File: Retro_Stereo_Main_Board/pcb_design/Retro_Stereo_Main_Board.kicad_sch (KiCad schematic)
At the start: 2 parts, among them J1 Conn_02x15_Counter_Clockwise, U3 TPS65132WRVCR

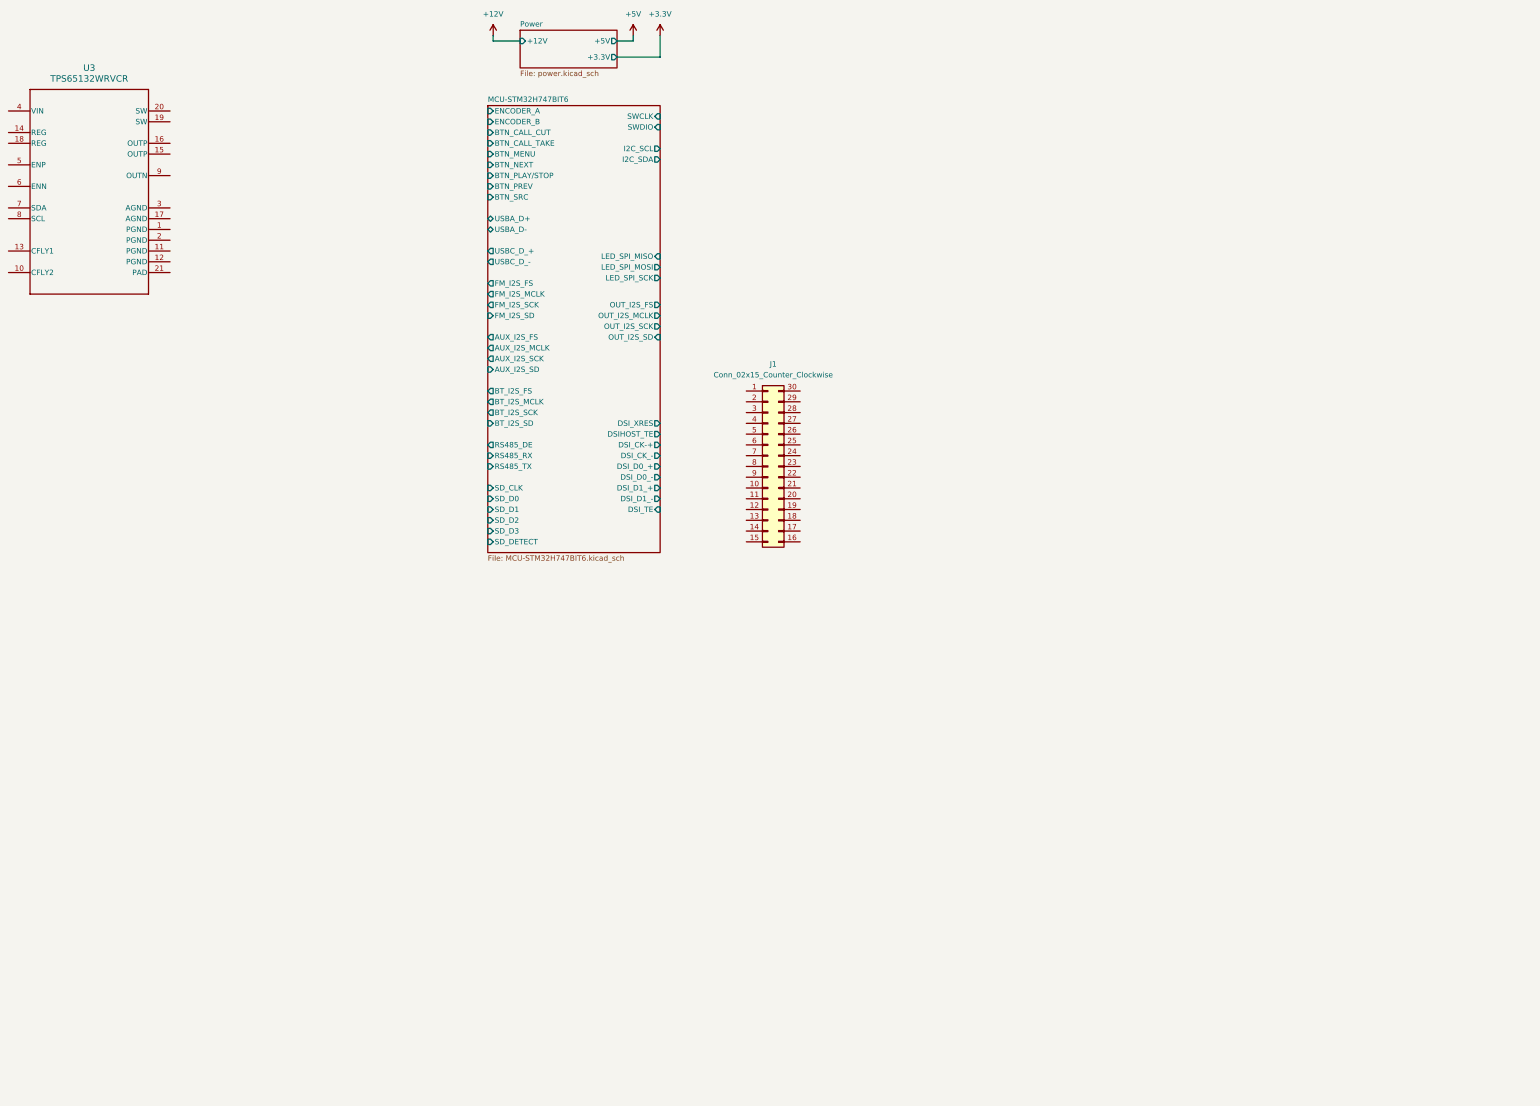
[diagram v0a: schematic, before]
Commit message: Define crystals, add peripherals
Signed-off-by: Francisco <fran.testa07Qgmail.com>
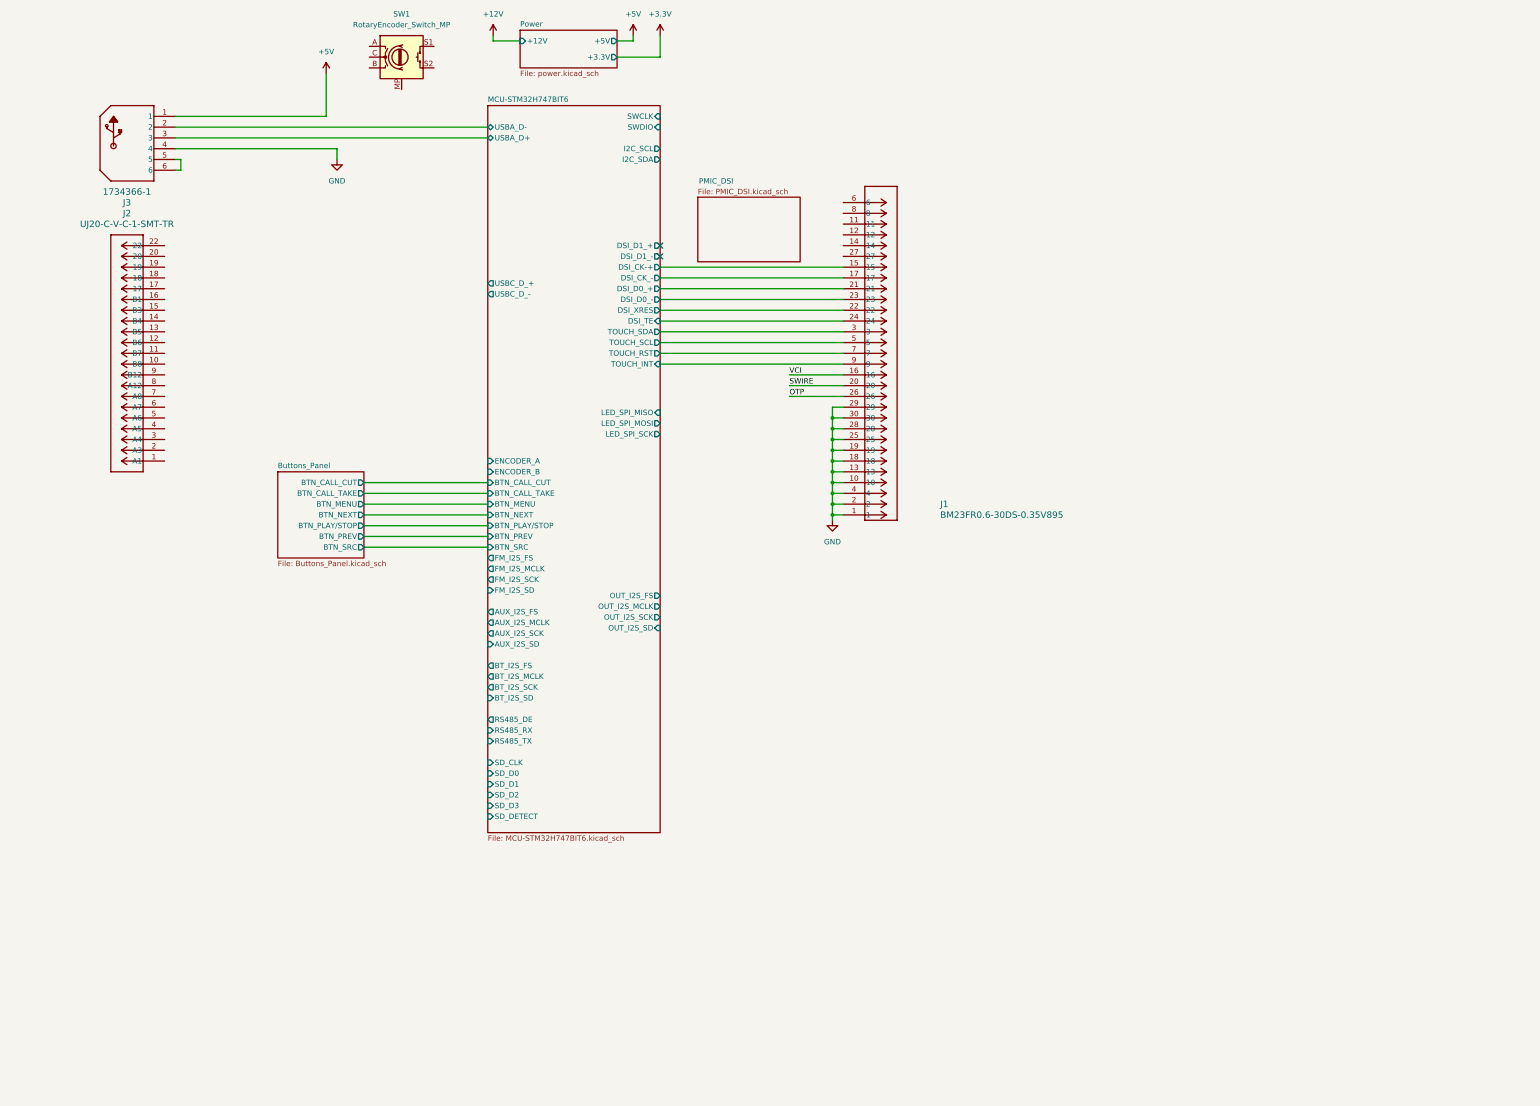
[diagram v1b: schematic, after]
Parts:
- removed J1: Conn_02x15_Counter_Clockwise, symbol Connector_Generic:Conn_02x15_Counter_Clockwise
- removed U3: TPS65132WRVCR, RVC0020A, symbol TPS65132WRVCR:TPS65132WRVCR
- added J1: BM23FR0.6-30DS-0.35V895, CONN_BM23FR0.6-30DS-0.35V895_HIR, symbol BM23FR0.6-30DS-0.35V(895):BM23FR0.6-30DS-0.35V895
- added J2: UJ20-C-V-C-1-SMT-TR, CONN8X2_UJ20-C-V-C-1-SMT-TR_CUD, symbol USBC_Samesky:UJ20-C-V-C-1-SMT-TR
- added J3: 1734366-1, CONN4_1734366-1_TEC, symbol USBA_TE:1734366-1
- added SW1: RotaryEncoder_Switch_MP, symbol Device:RotaryEncoder_Switch_MP
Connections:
- net +5V: now also J3.1
- net MCU-STM32H747BIT6/DSI_CK-+: now also J1.15
- net MCU-STM32H747BIT6/DSI_CK_-: now also J1.17
- net MCU-STM32H747BIT6/DSI_D0_+: now also J1.21
- net MCU-STM32H747BIT6/DSI_D0_-: now also J1.23
- net MCU-STM32H747BIT6/DSI_TE: now also J1.24
- net MCU-STM32H747BIT6/DSI_XRES: now also J1.22
- net MCU-STM32H747BIT6/USBA_D+: now also J3.3
- net MCU-STM32H747BIT6/USBA_D-: now also J3.2
- new net: J3.5, J3.6
- new net GND: J1.1, J1.10, J1.13, J1.18, J1.19, J1.2, J1.25, J1.28, J1.29, J1.30, J1.4, J3.4
- new net MCU-STM32H747BIT6/TOUCH_INT: J1.9
- new net MCU-STM32H747BIT6/TOUCH_RST: J1.7
- new net MCU-STM32H747BIT6/TOUCH_SCL: J1.5
- new net MCU-STM32H747BIT6/TOUCH_SDA: J1.3
- new net OTP: J1.26
- new net SWIRE: J1.20
- new net VCI: J1.16
- no-connect marks 0 -> 2
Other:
- added sheet Buttons_Panel (Buttons_Panel.kicad_sch)
- added sheet PMIC_DSI (PMIC_DSI.kicad_sch)
- sheet MCU-STM32H747BIT6 ports: added TOUCH_INT, TOUCH_RST, TOUCH_SCL, TOUCH_SDA; removed DSIHOST_TE

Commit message: Complete connections to display, add power block
Signed-off-by: Francisco <fran.testa07Qgmail.com>
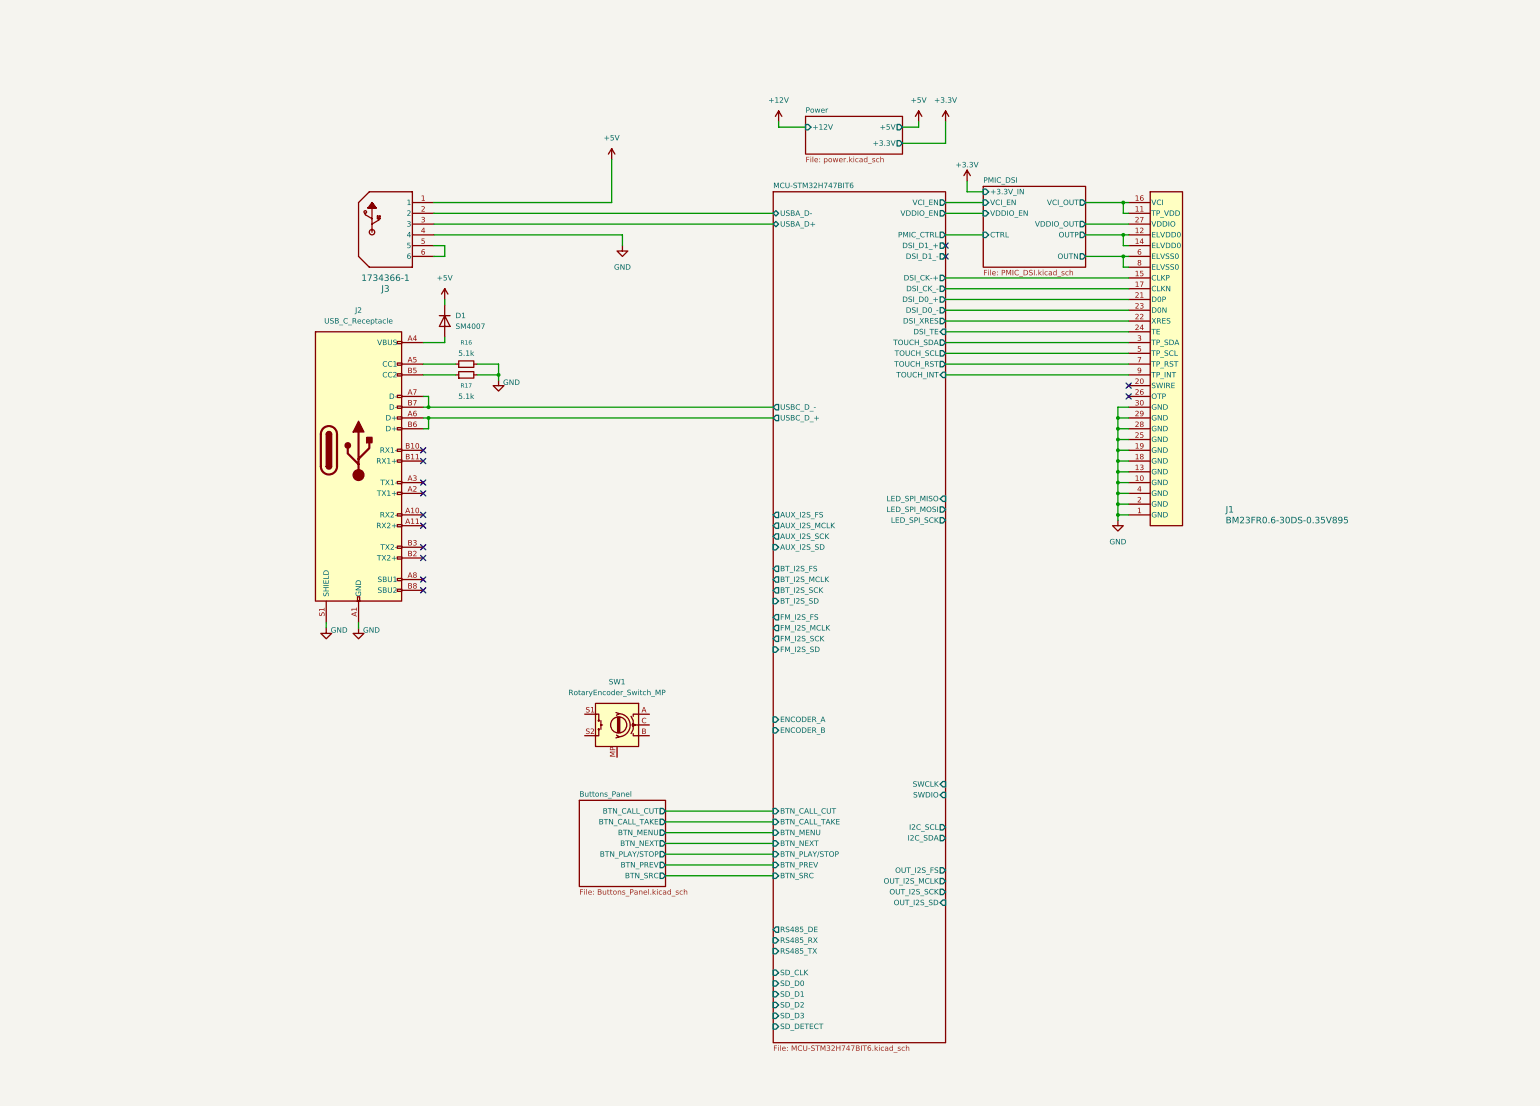
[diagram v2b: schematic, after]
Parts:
- removed J2: UJ20-C-V-C-1-SMT-TR, CONN8X2_UJ20-C-V-C-1-SMT-TR_CUD, symbol USBC_Samesky:UJ20-C-V-C-1-SMT-TR
- added D1: SM4007, Diode_SMD:D_SOD-123F, symbol Device:D
- added J2: USB_C_Receptacle, USBC_Samesky:CONN8X2_UJ20-C-V-C-1-SMT-TR_CUD, symbol Connector:USB_C_Receptacle
- added R16, R17: 5.1k, symbol Device:R_Small
- J3: footprint CONN4_1734366-1_TEC -> USBA_TE:CONN4_1734366-1_TEC
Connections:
- net VCI is gone; now on net PMIC_DSI/VCI_OUT: J1.16 (VCI)
- net +5V: now also D1.1 (K)
- net GND: now also J2.A1 (GND), J2.A12 (GND), J2.B1 (GND), J2.B12 (GND), J2.S1 (SHIELD), R16.2, R17.2
- net MCU-STM32H747BIT6/USBC_D_+: now also J2.A6 (D+), J2.B6 (D+)
- net MCU-STM32H747BIT6/USBC_D_-: now also J2.A7 (D-), J2.B7 (D-)
- net PMIC_DSI/VCI_OUT: now reaches J1.11 (TP_VDD)
- net PMIC_DSI/OUTP: now reaches J1.12 (ELVDD0)
- net PMIC_DSI/OUTP: now also J1.14 (ELVDD0)
- net PMIC_DSI/VDDIO_OUT: now reaches J1.27 (VDDIO)
- net PMIC_DSI/OUTN: now reaches J1.6 (ELVSS0)
- net PMIC_DSI/OUTN: now also J1.8 (ELVSS0)
- net OTP: no longer names the net of J1.26 (OTP)
- net SWIRE: no longer names the net of J1.20 (SWIRE)
- new net: J2.B5 (CC2), R17.1
- new net: D1.2 (A), J2.A4 (VBUS), J2.A9 (VBUS), J2.B4 (VBUS), J2.B9 (VBUS)
- new net: J2.A5 (CC1), R16.1
- no-connect marks 2 -> 14
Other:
- sheet MCU-STM32H747BIT6 ports: added PMIC_CTRL, VCI_EN, VDDIO_EN; removed none
- sheet PMIC_DSI ports: added +3.3V_IN, CTRL, OUTN, OUTP, VCI_EN, VCI_OUT, VDDIO_EN, VDDIO_OUT; removed none
- moved on the sheet: J3, SW1

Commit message: Add Aux port interface
- Also add bluetooth interface IC

Signed-off-by: Francisco <fran.testa07Qgmail.com>
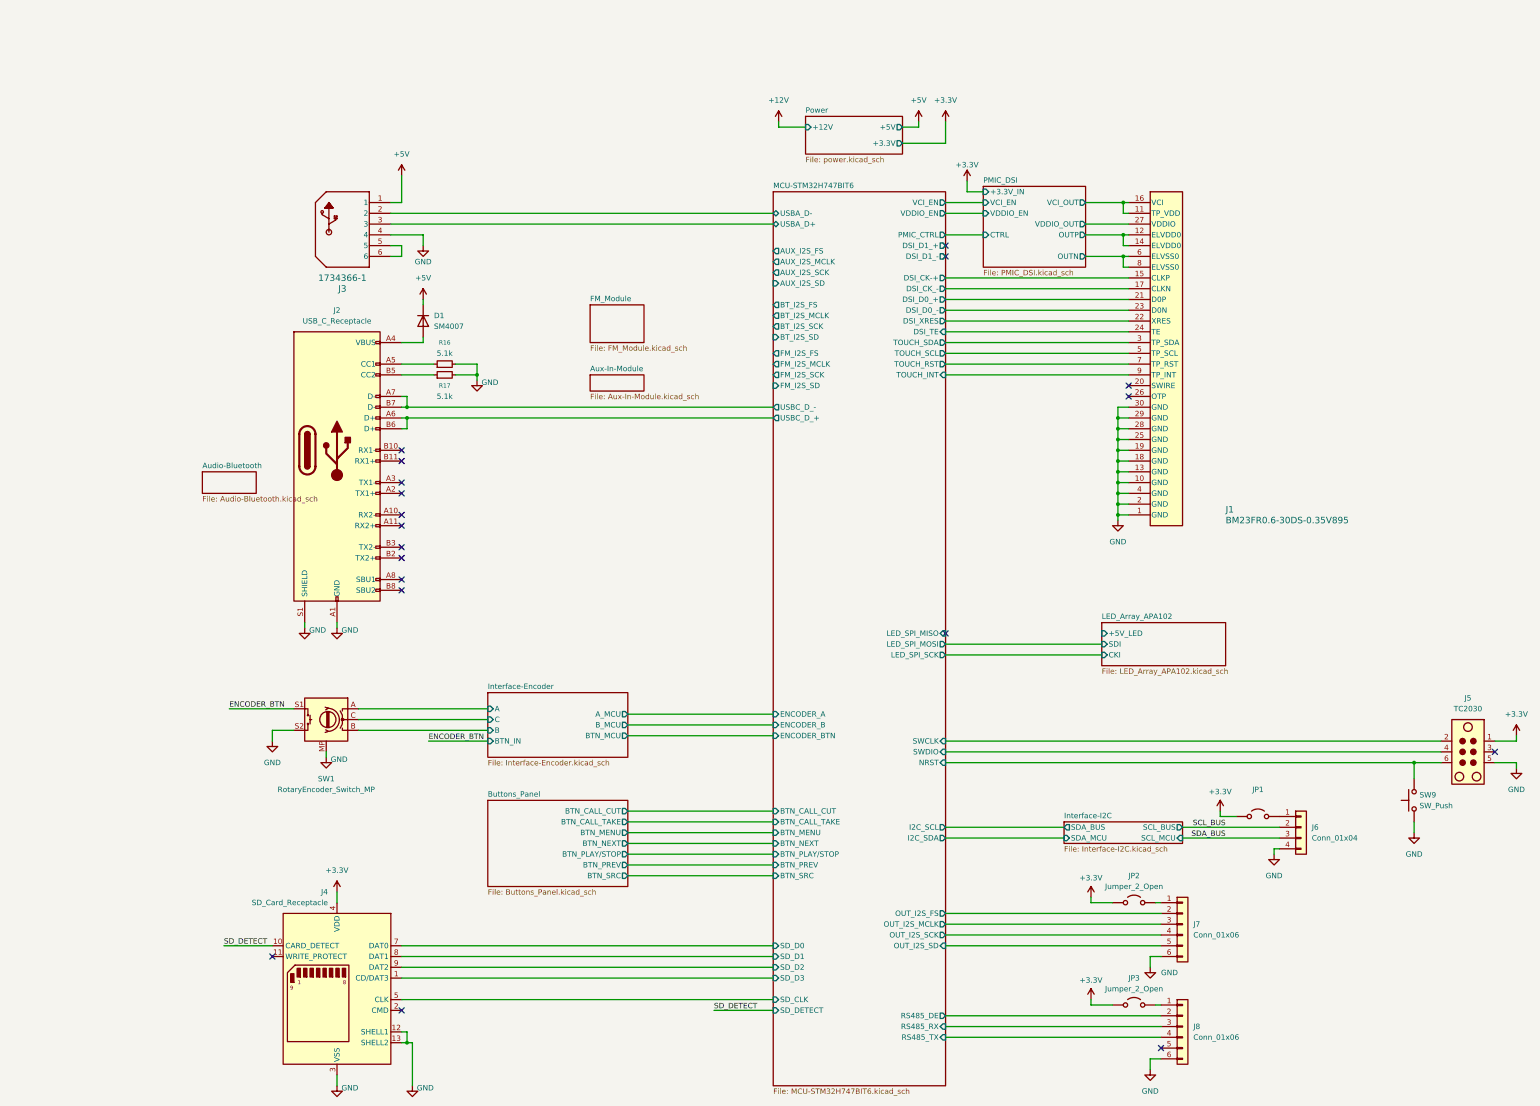
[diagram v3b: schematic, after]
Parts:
- added J4: SD_Card_Receptacle, symbol Connector:SD_Card_Receptacle
- added J5: TC2030, Connector:Tag-Connect_TC2030-IDC-NL_2x03_P1.27mm_Vertical, symbol Connector:TC2030
- added J6: Conn_01x04, symbol Connector_Generic:Conn_01x04
- added J7, J8: Conn_01x06, symbol Connector_Generic:Conn_01x06
- added JP1, JP2, JP3: Jumper_2_Open, symbol Jumper:Jumper_2_Open
- added SW9: SW_Push, symbol Switch:SW_Push
- SW1: MPN (none) -> PEC11R-4220F-S0024
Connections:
- net +3.3V: now also J4.4 (VDD), J5.1, JP1.1 (A), JP2.1 (A), JP3.1 (A)
- net GND: now also SW1.MP, SW1.S2, J4.12 (SHELL1), J4.13 (SHELL2), J4.3 (VSS), J4.6 (VSS), J5.5, J6.4 (Pin_4), J7.6 (Pin_6), J8.6 (Pin_6), SW9.1
- net MCU-STM32H747BIT6/OUT_I2S_FS: now also J7.2 (Pin_2)
- net MCU-STM32H747BIT6/OUT_I2S_MCLK: now also J7.3 (Pin_3)
- net MCU-STM32H747BIT6/OUT_I2S_SCK: now also J7.4 (Pin_4)
- net MCU-STM32H747BIT6/OUT_I2S_SD: now also J7.5 (Pin_5)
- net MCU-STM32H747BIT6/RS485_DE: now also J8.2 (Pin_2)
- net MCU-STM32H747BIT6/RS485_RX: now also J8.3 (Pin_3)
- net MCU-STM32H747BIT6/RS485_TX: now also J8.4 (Pin_4)
- net MCU-STM32H747BIT6/SD_CLK: now also J4.5 (CLK)
- net MCU-STM32H747BIT6/SD_D0: now also J4.7 (DAT0)
- net MCU-STM32H747BIT6/SD_D1: now also J4.8 (DAT1)
- net MCU-STM32H747BIT6/SD_D2: now also J4.9 (DAT2)
- net MCU-STM32H747BIT6/SD_D3: now also J4.1 (CD/DAT3)
- net MCU-STM32H747BIT6/SWCLK: now also J5.2
- net MCU-STM32H747BIT6/SWDIO: now also J5.4
- net Interface-Encoder/A: now reaches SW1.A
- net Interface-Encoder/B: now reaches SW1.B
- net Interface-Encoder/C: now reaches SW1.C
- net ENCODER_BTN: now reaches SW1.S1
- new net: J7.1 (Pin_1), JP2.2 (B)
- new net: J8.1 (Pin_1), JP3.2 (B)
- new net: J6.1 (Pin_1), JP1.2 (B)
- new net MCU-STM32H747BIT6/NRST: J5.6, SW9.2
- new net SCL_BUS: J6.2 (Pin_2)
- new net SDA_BUS: J6.3 (Pin_3)
- new net SD_DETECT: J4.10 (CARD_DETECT)
- no-connect marks 14 -> 19
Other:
- added sheet Audio-Bluetooth (Audio-Bluetooth.kicad_sch)
- added sheet Aux-In-Module (Aux-In-Module.kicad_sch)
- added sheet FM_Module (FM_Module.kicad_sch)
- added sheet Interface-Encoder (Interface-Encoder.kicad_sch)
- added sheet Interface-I2C (Interface-I2C.kicad_sch)
- added sheet LED_Array_APA102 (LED_Array_APA102.kicad_sch)
- sheet MCU-STM32H747BIT6 ports: added ENCODER_BTN, NRST; removed none
- moved on the sheet: D1, J2, J3, R16, R17, SW1

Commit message: Complete TEF6686 schematic page
- Start Bluetooth input design

Signed-off-by: Francisco <fran.testa07Qgmail.com>
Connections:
- no-connect marks 19 -> 21
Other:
- removed sheet Aux-In-Module
- sheet FM_Module ports: added ANT_IN, GPIO_0, GPIO_1, GPIO_2, I2S_BCK, I2S_SD_0, I2S_SD_1, I2S_WS, SCL_IN, SDA_IN; removed none
- sheet MCU-STM32H747BIT6 ports: added FM_GPIO_0, FM_GPIO_1, FM_GPIO_2; removed none

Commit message: Complete BT module sheet
Signed-off-by: Francisco <fran.testa07Qgmail.com>
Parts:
- added MK1: Microphone, symbol Device:Microphone
- added R44, R45, R46, R47: R_Small, symbol Device:R_Small
- added TP1, TP10, TP2, TP3, TP4, TP5, TP8, TP9: TestPoint, symbol Connector:TestPoint
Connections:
- net MCU-STM32H747BIT6/USBC_D_+: now also R44.2; no longer J2.A6 (D+), J2.B6 (D+)
- net MCU-STM32H747BIT6/USBC_D_-: now also R45.2; no longer J2.A7 (D-), J2.B7 (D-)
- new net Audio-Bluetooth/MIC_N1: MK1.2 (+)
- new net Audio-Bluetooth/MIC_P1: MK1.1 (-)
- new net Audio-Bluetooth/P0_1: TP1.1
- new net Audio-Bluetooth/P0_2: TP2.1
- new net Audio-Bluetooth/P0_3: TP3.1
- new net Audio-Bluetooth/P0_5: TP4.1
- new net Audio-Bluetooth/P1_6: TP5.1
- new net Audio-Bluetooth/P2_3: TP8.1
- new net Audio-Bluetooth/P2_6: TP9.1
- new net Audio-Bluetooth/P2_7: TP10.1
- new net Audio-Bluetooth/USB_D+: R46.2
- new net Audio-Bluetooth/USB_D-: R47.2
- new net USB_D+: J2.A7 (D-), J2.B7 (D-), R45.1, R46.1
- new net USB_D-: J2.A6 (D+), J2.B6 (D+), R44.1, R47.1
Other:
- sheet Audio-Bluetooth ports: added AUX_IN_L, AUX_IN_R, AUX_JACK_DET, I2C_SCL, I2C_SDA, I2S_BCLK, I2S_LRCLK, I2S_MCLK, I2S_SD, MFB, MIC_N1, MIC_P1, P0_1, P0_2, P0_3, P0_5, P1_6, P2_3, P2_6, P2_7, RST_IN, UART_CTS, UART_RTS, UART_RXD, UART_TXD, UART_TX_IND, USB_D+, USB_D-; removed none
- moved on the sheet: D1, J2, R16, R17, SW1
